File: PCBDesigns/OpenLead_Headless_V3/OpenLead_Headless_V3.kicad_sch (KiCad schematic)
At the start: 37 parts, among them J1 Conn_01x01, J2 Conn_01x01, J3 Conn_01x07_Pin, J4 Battery, J5 Conn_01x01, J6 Conn_01x07_Pin, Q1 AO3400A MOSFET, SW1 SW_DIP_x04, U3 TL431DBZ

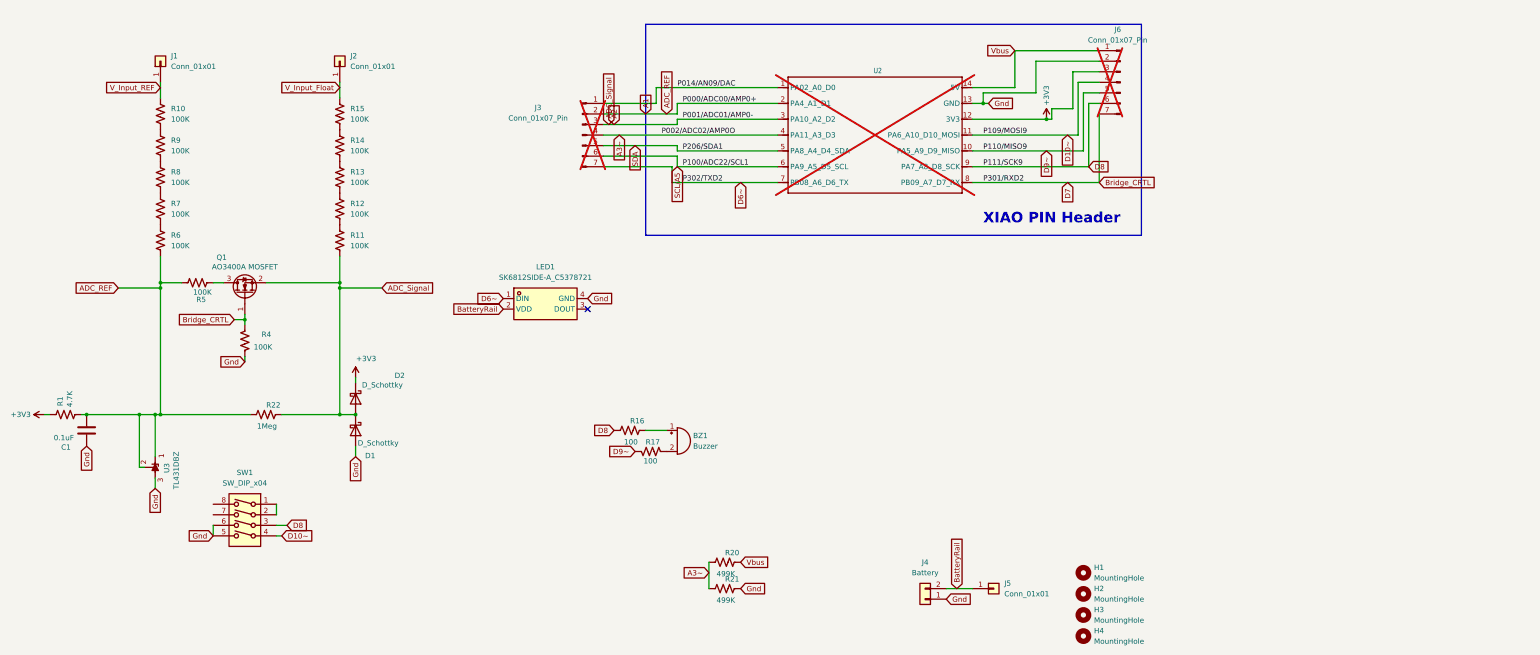
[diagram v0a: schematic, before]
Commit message: Blinky Hawk now has a low power sleep mode (1mA draw).
Wakes on activity, samples for activity every 1 second.

Fully configurable in the GUI.
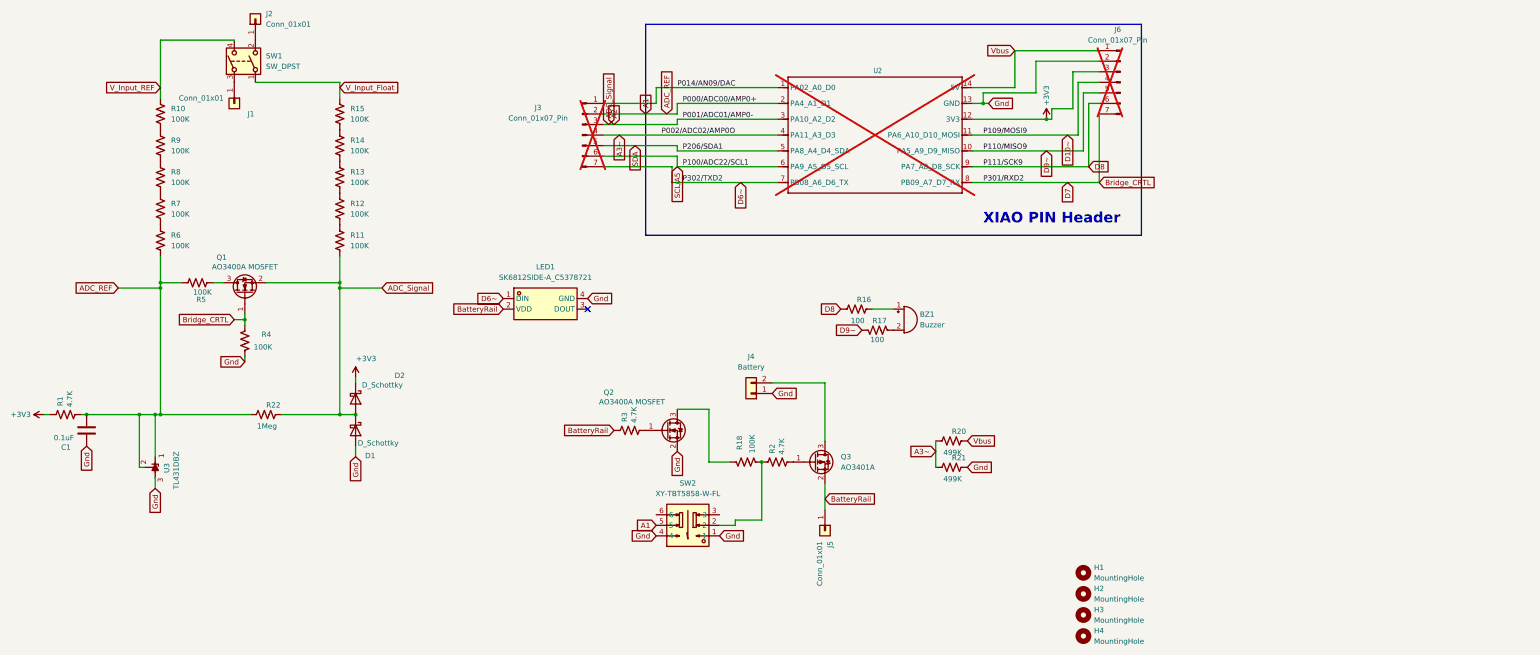
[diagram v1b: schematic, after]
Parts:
- removed SW1: SW_DIP_x04, Button_Switch_SMD:SW_DIP_SPSTx04_Slide_KingTek_DSHP04TS_W7.62mm_P1.27mm, symbol Switch:SW_DIP_x04
- added Q2: AO3400A MOSFET, Package_TO_SOT_SMD:SOT-23, symbol Transistor_FET:DMG2302U
- added Q3: AO3401A, Package_TO_SOT_SMD:SOT-23, symbol Transistor_FET:AO3401A
- added R18: 100K, Resistor_SMD:R_0805_2012Metric, symbol Device:R_US
- added R2, R3: 4.7K, Resistor_SMD:R_0805_2012Metric, symbol Device:R_US
- added SW1: SW_DPST, symbol Switch:SW_DPST
- added SW2: XY-TBT5858-W-FL, easyeda_parts:SW-SMD_6P-L5.8-W5.8-P2.00-LS11.3-1, symbol CustomLibrary:XY-TBT5858-W-FL
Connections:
- net A1: now also SW2.5
- net BatteryRail: now also Q3.2 (S), R3.1; no longer J4.2 (Pin_2)
- net Gnd: now also Q2.2 (S), SW2.1, SW2.4
- net V_Input_Float: now also SW1.1; no longer J2.1 (Pin_1)
- net V_Input_REF: now also SW1.4; no longer J1.1 (Pin_1)
- new net: Q3.1 (G), R2.2
- new net: J4.2 (Pin_2), Q3.3 (D)
- new net: J2.1 (Pin_1), SW1.2
- new net: J1.1 (Pin_1), SW1.3
- new net: R18.1, R2.1, SW2.2
- new net: Q2.3 (D), R18.2
- new net: Q2.1 (G), R3.2
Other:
- moved on the sheet: BZ1, J1, J2, J4, J5, R16, R17, R20, R21

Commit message: BlinkyHawk PCB V3 Firmware is now a thing
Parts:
- removed SW1: SW_DPST, symbol Switch:SW_DPST
- H1, H2, H3, H4, J5, Q2, Q3, R18, R2, R3, SW2: now not fitted
- J1, J2: footprint Connector_Wire:SolderWire-0.75sqmm_1x01_D1.25mm_OD2.3mm -> Connector_Wire:SolderWirePad_1x01_SMD_1.5x3mm
- R20, R21: value 499K -> 100K
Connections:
- net A1: no longer C1.2, R1.2, R22.1, R5.2, R6.2, U3.1 (K), U3.2 (REF)
- net BatteryRail: now also J4.2 (Pin_2)
- net V_Input_Float: now also J2.1 (Pin_1)
- net V_Input_REF: now also J1.1 (Pin_1)
- net at Q3.3 (D): no longer J4.2 (Pin_2)
- new net: C1.2, R1.2, R22.1, R5.2, R6.2, U3.1 (K), U3.2 (REF)
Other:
- moved on the sheet: J1, J2, R20, R21
